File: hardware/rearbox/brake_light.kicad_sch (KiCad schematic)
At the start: 5 parts, among them Q1 PMV164ENE

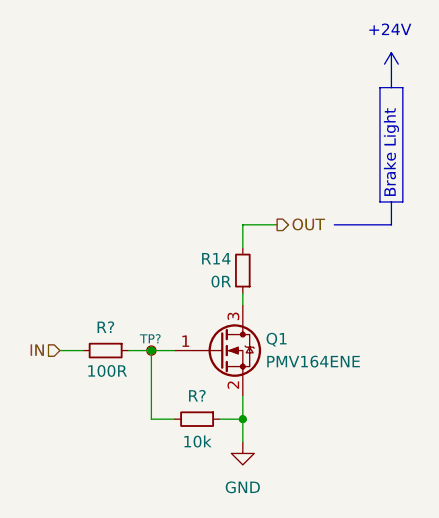
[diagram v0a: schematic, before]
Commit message: Place components on the PCB
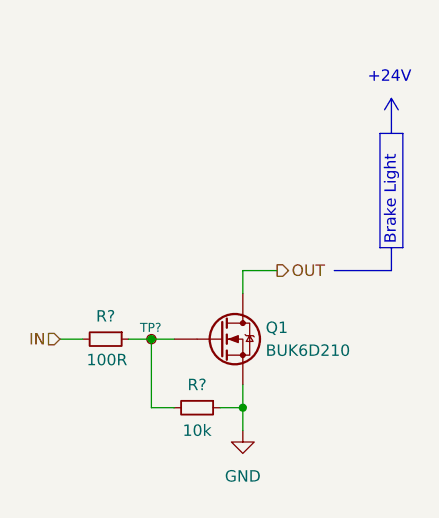
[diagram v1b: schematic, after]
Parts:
- removed Q1: PMV164ENE, Package_TO_SOT_SMD:SOT-23, symbol Device:Q_NMOS_GSD
- removed R14: 0R, Resistor_SMD:R_0603_1608Metric, symbol Device:R_Small
- added Q1: BUK6D210, Package_DFN_QFN:Diodes_UDFN2020-6_Type-F, symbol BUK6D210:BUK6D210
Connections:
- net GND: now also Q1.4 (S), Q1.8 (S)
- net OUT: now also Q1.1 (D), Q1.2 (D), Q1.5 (D), Q1.6 (D), Q1.7 (D)
- net at R?.1, R?.2, TP?.1: now also Q1.3 (G)
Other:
- moved on the sheet: R?, TP?

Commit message: Route PCB tracks
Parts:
- Q1: footprint Package_DFN_QFN:Diodes_UDFN2020-6_Type-F -> Local_Library:Diodes_UDFN2020-6_Type-F
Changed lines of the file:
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@@
       (effects (font (size 1.27 1.27)) (justify left))
     )
-    (property "Footprint" "Package_DFN_QFN:Diodes_UDFN2020-6_Type-F" (at 151.13 118.11 0)
+    (property "Footprint" "Local_Library:Diodes_UDFN2020-6_Type-F" (at 151.13 118.11 0)
       (effects (font (size 1.27 1.27)) hide)
     )

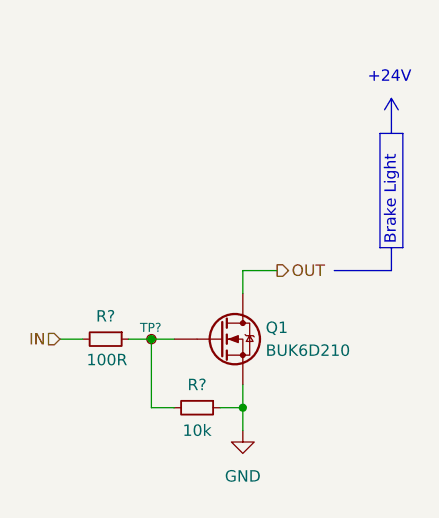
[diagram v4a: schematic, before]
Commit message: Route the tracks on the connector PCB
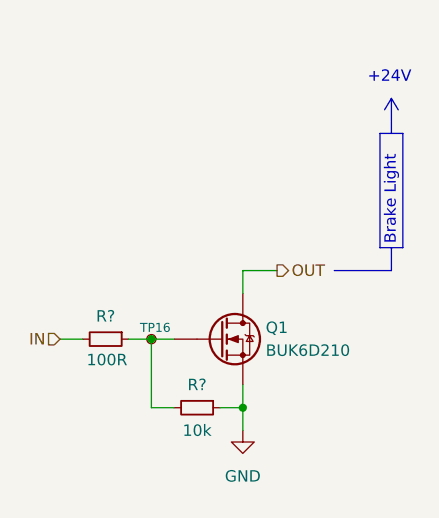
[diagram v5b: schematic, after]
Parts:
- gave numbers to parts that had none: 1
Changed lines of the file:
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@@
       )
       (project "rearbox"
-        (path "/b652b05a-4e3d-4ad1-b032-18886abe7d45/23ffbfb4-d932-48bb-a16b-e7ed705895f1"
-          (reference "R?") (unit 1)
-        )
         (path "/b652b05a-4e3d-4ad1-b032-18886abe7d45/91248db3-ac16-4fb7-9cfe-25145bb94249"
           (reference "R9") (unit 1)
@@
   (symbol (lib_id "Connector:TestPoint_Small") (at 142.24 105.41 0) (unit 1)
     (in_bom yes) (on_board yes) (dnp no)
-    (property "Reference" "TP?" (at 140.97 104.14 0)
+    (property "Reference" "TP16" (at 140.97 104.14 0)
       (effects (font (size 1 1)) (justify left))
     )
@@
     (instances
       (project "rearbox"
-        (path "/b652b05a-4e3d-4ad1-b032-18886abe7d45/38408e41-dfb1-4c27-acb0-3f1224cc8789"
-          (reference "TP?") (unit 1)
-        )
-        (path "/b652b05a-4e3d-4ad1-b032-18886abe7d45/38408e41-dfb1-4c27-acb0-3f1224cc8789/eec2c93a-0fce-4d3a-ab43-9e1e0481c06c"
-          (reference "TP3") (unit 1)
-        )
-        (path "/b652b05a-4e3d-4ad1-b032-18886abe7d45/38408e41-dfb1-4c27-acb0-3f1224cc8789/f1ed15a3-9302-436f-b25a-713477aeadf3"
-          (reference "TP1") (unit 1)
-        )
         (path "/b652b05a-4e3d-4ad1-b032-18886abe7d45/91248db3-ac16-4fb7-9cfe-25145bb94249"
           (reference "TP16") (unit 1)
@@
       )
       (project "rearbox"
-        (path "/b652b05a-4e3d-4ad1-b032-18886abe7d45/23ffbfb4-d932-48bb-a16b-e7ed705895f1"
-          (reference "R?") (unit 1)
-        )
         (path "/b652b05a-4e3d-4ad1-b032-18886abe7d45/91248db3-ac16-4fb7-9cfe-25145bb94249"
           (reference "R8") (unit 1)
@@
           (reference "Q1") (unit 1)
         )
-        (path "/b652b05a-4e3d-4ad1-b032-18886abe7d45/562e38ba-d94a-4627-8fa0-e9eb7b5e4e9a"
-          (reference "Q10") (unit 1)
-        )
-        (path "/b652b05a-4e3d-4ad1-b032-18886abe7d45/12f12a63-cabc-40cf-a64b-d1bd8b3dd459"
-          (reference "Q12") (unit 1)
-        )
-        (path "/b652b05a-4e3d-4ad1-b032-18886abe7d45/2f82735d-d185-44cc-bb86-fc399780134d"
-          (reference "Q4") (unit 1)
-        )
-        (path "/b652b05a-4e3d-4ad1-b032-18886abe7d45/23ffbfb4-d932-48bb-a16b-e7ed705895f1"
-          (reference "Q4") (unit 1)
-        )
       )
